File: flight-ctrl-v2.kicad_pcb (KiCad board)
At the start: 2 copper layers, 45 x 45 mm, 45 parts, among them J1 ESC1, J2 ESC2, J3 ESC3, J4 ESC4, J5 RECEIVER, J6 SERIAL, J7 SWD, U1 LD3985M33R, U2 STM32F405RG-LQFP64, U3 LSM9DS1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

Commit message: added swd resistors to pcb
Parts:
- added R3: 10k, footprints:RC0402FR-0710KL, F.Cu at (140.0, 130.9)
- added R4: 10k, footprints:RC0402FR-0710KL, F.Cu at (141.6, 130.9)
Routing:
- net GND: track 268.6 -> 278.2 mm
- net SWDIO: track 55.1 -> 61.0 mm
- net +3V3: track 170.5 -> 173.4 mm, vias 10 -> 11
- net SWCLK: track 51.3 -> 54.0 mm, vias 3 -> 4

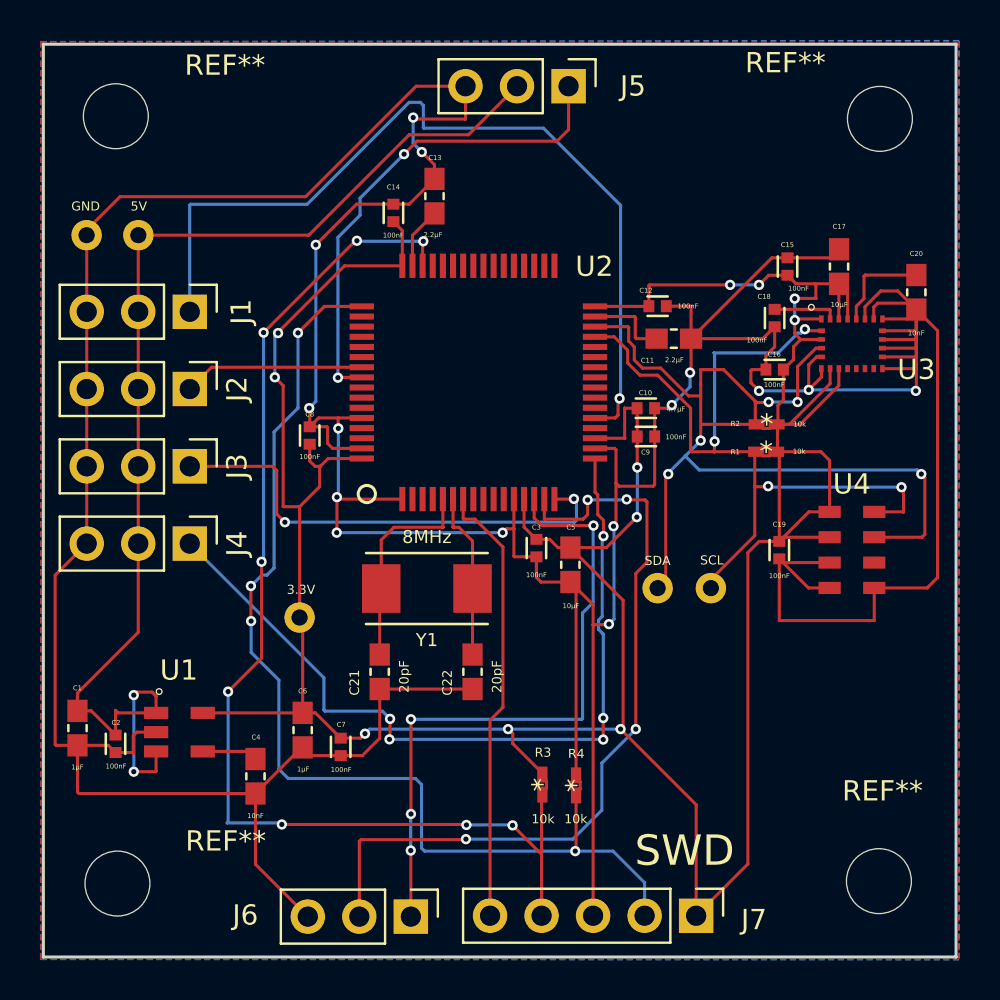
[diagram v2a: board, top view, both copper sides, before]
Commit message: added ferrite bead as filter for VDDA
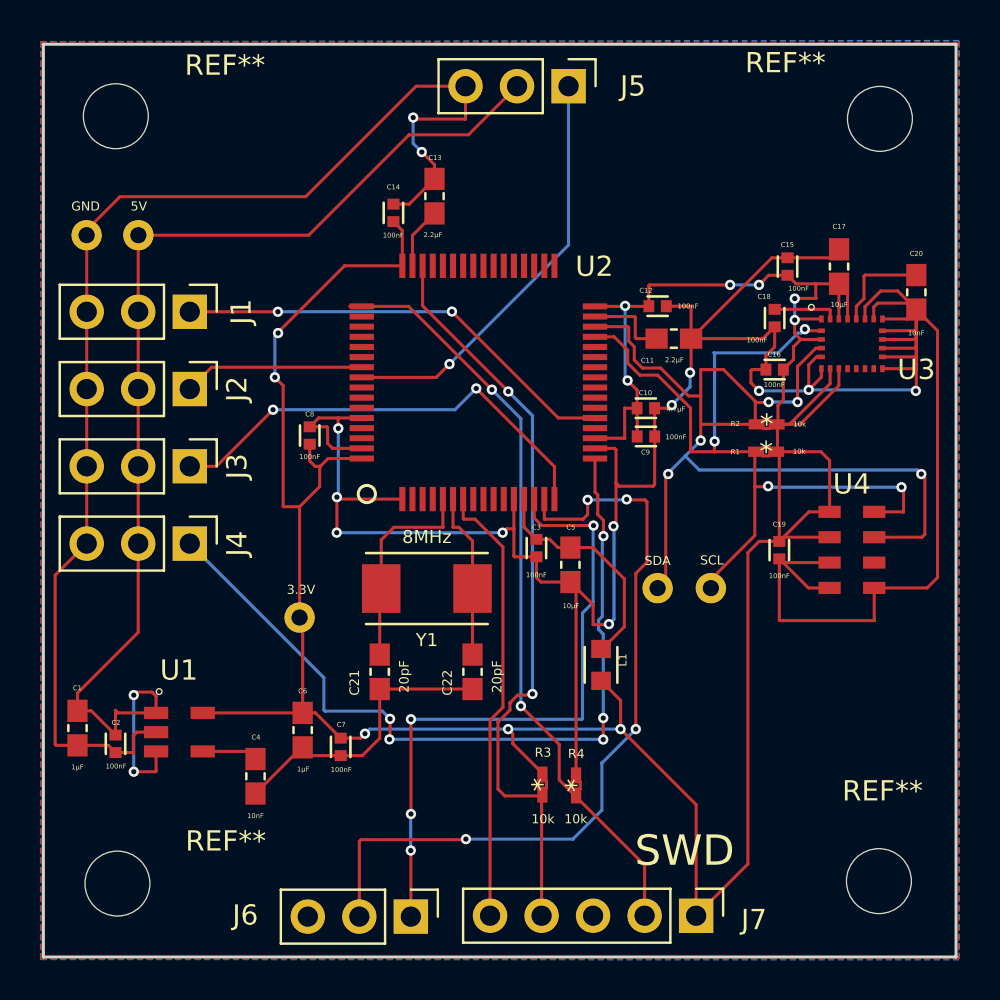
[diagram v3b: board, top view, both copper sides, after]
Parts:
- added L1: BK1608HS601-T, BK1608HS601-T:BEADC1608X95N, F.Cu at (142.9, 125.0)
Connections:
- C3 pad 1: +3V3 -> Net-(C3-Pad1)
- C5 pad 1: +3V3 -> Net-(C3-Pad1)
- U2 pad 13: +3V3 -> Net-(C3-Pad1)
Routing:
- net GND: track 278.2 -> 231.8 mm, vias 15 -> 13
- net SWDIO: track 61.0 -> 37.4 mm, vias 8 -> 2
- net TIM2_CH1: track 42.9 -> 22.2 mm, vias 1 -> 2
- net SWCLK: track 54.0 -> 37.8 mm, vias 4 -> 2
- net +3V3: track 173.4 -> 158.9 mm
- net Net-(C3-Pad1): track 0.00 -> 11.9 mm
- net TIM3_CH1: track 24.3 -> 20.7 mm, vias 2 -> 1
- net TIM2_CH3: track 23.6 -> 22.8 mm

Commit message: connected VBAT to VDD instead of GND
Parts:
- added C23: 100nF, CC0402ZRY5V7BB104:CAPC1005X55N, F.Cu at (139.3, 122.3)
- added R5: 100k, RC0402FR07100KL:RC0402FR-07100KL, F.Cu at (139.6, 124.6)
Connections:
- U2 pad 1: GND -> +3V3
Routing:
- net +3V3: track 158.9 -> 166.2 mm, vias 11 -> 12
- net RESET: track 21.9 -> 23.9 mm
- net GND: track 231.8 -> 230.4 mm
